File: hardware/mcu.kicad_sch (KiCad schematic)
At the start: 36 parts, among them U1 74LVC125, U2 STM32F407VETx, U3 24LC64, U7 74LVC125, X1 12MHz

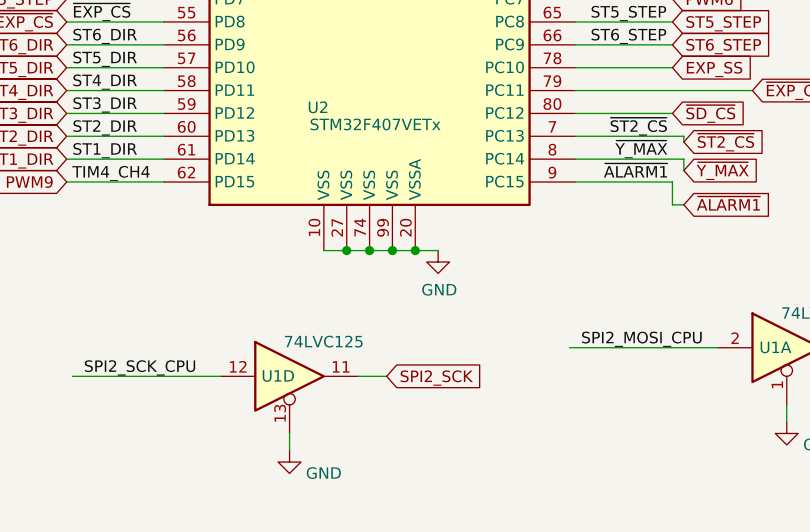
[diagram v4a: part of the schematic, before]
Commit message: Added separate power supply for motor drivers, to accomodate high voltage driver versions.
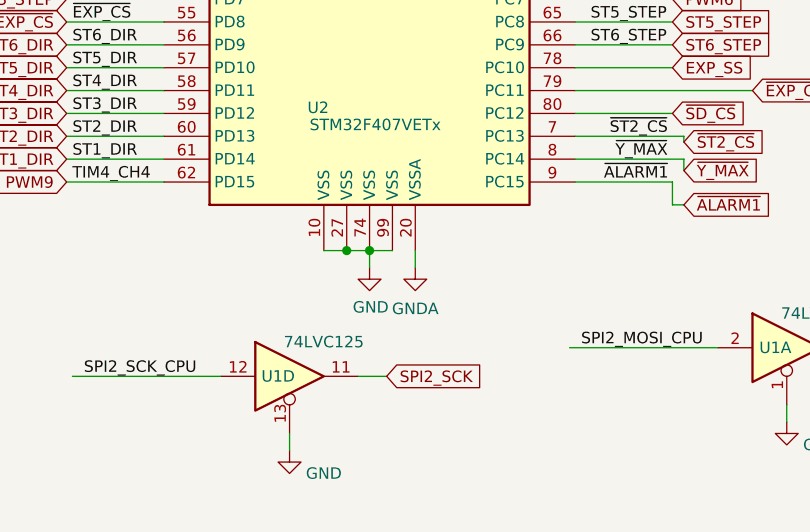
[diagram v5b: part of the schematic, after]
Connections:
- net GND: no longer U2.20 (VSSA)
- new net GNDA: U2.20 (VSSA)
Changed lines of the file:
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@@
   (junction (at 103.505 163.83) (diameter 1.016) (color 0 0 0 0))
   (junction (at 106.045 24.13) (diameter 1.016) (color 0 0 0 0))
-  (junction (at 106.045 163.83) (diameter 1.016) (color 0 0 0 0))
   (junction (at 108.585 24.13) (diameter 1.016) (color 0 0 0 0))
-  (junction (at 108.585 163.83) (diameter 1.016) (color 0 0 0 0))
   (junction (at 111.125 24.13) (diameter 1.016) (color 0 0 0 0))
   (junction (at 113.665 20.32) (diameter 1.016) (color 0 0 0 0))
@@
     (stroke (width 0) (type solid) (color 0 0 0 0))
   )
+  (wire (pts (xy 103.505 163.83) (xy 103.505 165.735))
+    (stroke (width 0) (type default) (color 0 0 0 0))
+  )
   (wire (pts (xy 106.045 24.13) (xy 108.585 24.13))
     (stroke (width 0) (type solid) (color 0 0 0 0))
@@
     (stroke (width 0) (type solid) (color 0 0 0 0))
   )
-  (wire (pts (xy 108.585 163.83) (xy 106.045 163.83))
-    (stroke (width 0) (type solid) (color 0 0 0 0))
+  (wire (pts (xy 108.585 163.83) (xy 108.585 165.735))
+    (stroke (width 0) (type default) (color 0 0 0 0))
   )
   (wire (pts (xy 111.125 22.86) (xy 111.125 24.13))
-    (stroke (width 0) (type solid) (color 0 0 0 0))
-  )
-  (wire (pts (xy 111.125 163.83) (xy 108.585 163.83))
     (stroke (width 0) (type solid) (color 0 0 0 0))
   )
@@
     (pin "1")
   )
-  (symbol (lib_id "power:GND") (at 111.125 163.83 0) (unit 1)
+  (symbol (lib_id "power:GND") (at 103.505 165.735 0) (unit 1)
     (in_bom yes) (on_board yes)
-    (property "Reference" "#PWR03" (id 0) (at 111.125 170.18 0)
-      (effects (font (size 1.27 1.27)) hide)
-    )
-    (property "Value" "GND" (id 1) (at 111.252 168.2242 0))
-    (property "Footprint" "" (id 2) (at 111.125 163.83 0)
-      (effects (font (size 1.27 1.27)) hide)
-    )
-    (property "Datasheet" "" (id 3) (at 111.125 163.83 0)
-      (effects (font (size 1.27 1.27)) hide)
-    )
+    (property "Reference" "#PWR03" (id 0) (at 103.505 172.085 0)
+      (effects (font (size 1.27 1.27)) hide)
+    )
+    (property "Value" "GND" (id 1) (at 103.632 170.1292 0))
+    (property "Footprint" "" (id 2) (at 103.505 165.735 0)
+      (effects (font (size 1.27 1.27)) hide)
+    )
+    (property "Datasheet" "" (id 3) (at 103.505 165.735 0)
+      (effects (font (size 1.27 1.27)) hide)
+    )
+    (pin "1")
+  )
+  (symbol (lib_id "power:GNDA") (at 108.585 165.735 0) (unit 1)
+    (in_bom yes) (on_board yes) (fields_autoplaced)
+    (property "Reference" "#PWR0105" (id 0) (at 108.585 172.085 0)
+      (effects (font (size 1.27 1.27)) hide)
+    )
+    (property "Value" "GNDA" (id 1) (at 108.585 170.2976 0))
+    (property "Footprint" "" (id 2) (at 108.585 165.735 0)
+      (effects (font (size 1.27 1.27)) hide)
+    )
+    (property "Datasheet" "" (id 3) (at 108.585 165.735 0)
+      (effects (font (size 1.27 1.27)) hide)
+    )
